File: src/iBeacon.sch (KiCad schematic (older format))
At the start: 7 parts, among them IC1 AE-TYBLE16, P1 CONN_01X02, P2 CONN_01X02, P3 CONN_01X02

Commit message: 2nd Version
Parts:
- added IC2: ATTINY10-TSHR, ATTINY10-TSHR:SOT95P280X145-6N, symbol ATTINY10-TSHR
- added JP1: JUMPER, solderjumper:SolderJumper-2_P1.3mm_Open_Pad1.0x1.5mm, symbol JUMPER
- added P4: CONN_01X03, Pin_Headers:Pin_Header_Angled_1x03_Pitch2.54mm, symbol CONN_01X03
- D1: footprint LEDs:LED_1206_HandSoldering -> LEDs:LED_0603_HandSoldering
- R1: footprint Resistors_SMD:R_1206_HandSoldering -> Resistors_SMD:R_0603_HandSoldering
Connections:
- net at Battery1.1 (P1), IC1.11 (+V), P1.1 (P1): now also IC2.5 (VCC)
- net at Battery1.2 (P2), D1.1 (K), IC1.12 (GND)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: now also IC2.2 (GND)
- net at IC1.2 (SWDI), P2.1 (P1): now also JP1.2
- new net: IC2.4 (PB2_(T0/CLKO/PCINT2/INT0/ADC2)), JP1.1
- new net: IC2.1 ((PCINT0/TPIDATA/OC0A/ADC0/AIN0)_PB0), P4.2 (P2)
- new net: IC2.3 ((PCINT1/TPICLK/CLKI/ICP0/OC0B/ADC1/AIN1)_PB1), P4.1 (P1)
- new net: IC2.6 (PB3_(~RESET~/PCINT3/ADC3)), P4.3 (P3)
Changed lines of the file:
@@
 LIBS:valves
 LIBS:ae-tyble16
+LIBS:ATTINY10-TSHR
 LIBS:iBeacon-cache
 EELAYER 25 0
@@
 NoConn ~ 5150 3300
 NoConn ~ 5150 3500
-Wire Wire Line
-	4250 3400 4150 3400
-Wire Wire Line
-	4150 3400 4150 3500
-Wire Wire Line
-	4150 3500 4250 3500
 $Comp
 L CONN_01X02 Battery1
@@
 	1    0    0    -1
 $EndComp
-Wire Wire Line
-	4250 3000 4100 3000
-Wire Wire Line
-	4100 3000 4100 3100
-Wire Wire Line
-	4100 3100 3950 3100
-Wire Wire Line
-	3950 3200 4250 3200
-Wire Wire Line
-	4250 3300 3950 3300
-Wire Wire Line
-	4000 2900 4250 2900
-Wire Wire Line
-	5150 3000 5650 3000
-Wire Wire Line
-	5150 3100 5650 3100
-Wire Wire Line
-	5300 2400 5250 2400
-Wire Wire Line
-	5250 2400 5250 3000
-Connection ~ 5250 3000
-Wire Wire Line
-	5300 2500 5200 2500
-Wire Wire Line
-	5200 2500 5200 3100
-Connection ~ 5200 3100
 $Comp
 L AE-TYBLE16 IC1
@@
 F 0 "R1" V 5430 3400 50  0000 C CNN
 F 1 "R" V 5350 3400 50  0000 C CNN
-F 2 "Resistors_SMD:R_1206_HandSoldering" V 5280 3400 50  0000 C CNN
+F 2 "Resistors_SMD:R_0603_HandSoldering" V 5280 3400 50  0000 C CNN
 F 3 "" H 5350 3400 50  0000 C CNN
 	1    5350 3400
@@
 F 0 "D1" H 5750 3500 50  0000 C CNN
 F 1 "LED" H 5750 3300 50  0000 C CNN
-F 2 "LEDs:LED_1206_HandSoldering" H 5800 3250 50  0000 C CNN
+F 2 "LEDs:LED_0603_HandSoldering" H 5800 3250 50  0000 C CNN
 F 3 "" H 5750 3400 50  0000 C CNN
 	1    5750 3400
 	-1   0    0    -1
 $EndComp
-Wire Wire Line
-	5150 3400 5200 3400
-Wire Wire Line
-	5500 3400 5550 3400
-Wire Wire Line
-	5950 3200 5950 3400
-Wire Wire Line
-	5500 3200 5950 3200
-Wire Wire Line
-	5500 3100 5500 3200
-Connection ~ 5500 3100
 $Comp
 L CONN_01X02 P3
@@
 	1    0    0    -1
 $EndComp
+$Comp
+L JUMPER JP1
+U 1 1 5CA0BF62
+P 3800 2400
+F 0 "JP1" H 3800 2550 50  0000 C CNN
+F 1 "JUMPER" H 3800 2320 50  0000 C CNN
+F 2 "solderjumper:SolderJumper-2_P1.3mm_Open_Pad1.0x1.5mm" H 3800 2400 50  0000 C CNN
+F 3 "" H 3800 2400 50  0000 C CNN
+	1    3800 2400
+	1    0    0    -1
+$EndComp
+$Comp
+L ATTINY10-TSHR IC2
+U 1 1 5CA0BFA7
+P 1800 1350
+F 0 "IC2" H 6050 1650 50  0000 L CNN
+F 1 "ATTINY10-TSHR" H 6050 1550 50  0000 L CNN
+F 2 "ATTINY10-TSHR:SOT95P280X145-6N" H 6050 1450 50  0001 L CNN
+F 3 "http://www.atmel.com/images/atmel-8127-avr-8-bit-microcontroller-attiny4-attiny5-attiny9-attiny10_datasheet.pdf" H 6050 1350 50  0001 L CNN
+F 4 "ATTINY10-TSHR, 8 bit AVR Microcontroller 12MHz 1024 B Flash, 32 B RAM, 6-Pin SOT-23" H 6050 1250 50  0001 L CNN "Description"
+F 5 "1.45" H 6050 1150 50  0001 L CNN "Height"
+F 6 "Microchip" H 6050 1050 50  0001 L CNN "Manufacturer_Name"
+F 7 "ATTINY10-TSHR" H 6050 950 50  0001 L CNN "Manufacturer_Part_Number"
+F 8 "556-ATTINY10-TSHR" H 6050 850 50  0001 L CNN "Mouser Part Number"
+F 9 "https://www.mouser.com/Search/Refine.aspx?Keyword=556-ATTINY10-TSHR" H 6050 750 50  0001 L CNN "Mouser Price/Stock"
+F 10 "1330946P" H 6050 650 50  0001 L CNN "RS Part Number"
+F 11 "http://uk.rs-online.com/web/p/products/1330946P" H 6050 550 50  0001 L CNN "RS Price/Stock"
+	1    1800 1350
+	1    0    0    -1
+$EndComp
+Wire Wire Line
+	4250 3400 4150 3400
+Wire Wire Line
+	4150 3400 4150 3500
+Wire Wire Line
+	4150 3500 4250 3500
+Wire Wire Line
+	4250 3000 4100 3000
+Wire Wire Line
+	4100 3000 4100 3100
+Wire Wire Line
+	4100 3100 3950 3100
+Wire Wire Line
+	3950 3200 4250 3200
+Wire Wire Line
+	4250 3300 3950 3300
+Wire Wire Line
+	4000 2900 4250 2900
+Wire Wire Line
+	5150 3000 5650 3000
+Wire Wire Line
+	5150 3100 5650 3100
+Wire Wire Line
+	5300 2400 5250 2400
+Wire Wire Line
+	5250 2400 5250 3000
+Connection ~ 5250 3000
+Wire Wire Line
+	5300 2500 5200 2500
+Wire Wire Line
+	5200 2500 5200 3100
+Connection ~ 5200 3100
+Wire Wire Line
+	5150 3400 5200 3400
+Wire Wire Line
+	5500 3400 5550 3400
+Wire Wire Line
+	5950 3200 5950 3400
+Wire Wire Line
+	5500 3200 6700 3200
+Wire Wire Line
+	5500 3100 5500 3200
+Connection ~ 5500 3100
 Wire Wire Line
 	4000 2900 4000 3000
 Wire Wire Line
 	4000 3000 3950 3000
+Wire Wire Line
+	4100 2400 4100 2900
+Connection ~ 4100 2900
+Wire Wire Line
+	3500 2400 3500 1800
+Wire Wire Line
+	3500 1800 6200 1800
+Wire Wire Line
+	6200 1800 6200 1550
+Wire Wire Line
+	6200 1450 6350 1450
+Wire Wire Line
+	6350 1450 6350 2200
+Wire Wire Line
+	6350 2200 5600 2200
+Wire Wire Line
+	5600 2200 5600 2900
+Wire Wire Line
+	5600 2900 5500 2900
+Wire Wire Line
+	5500 2900 5500 3000
+Connection ~ 5500 3000
+Wire Wire Line
+	6700 3200 6700 950
+Wire Wire Line
+	6700 950  1550 950
+Wire Wire Line
+	1550 950  1550 1450
+Wire Wire Line
+	1550 1450 1800 1450
+Connection ~ 5950 3200
+$Comp
+L CONN_01X03 P4
+U 1 1 5CA0C661
+P 1400 2150
+F 0 "P4" H 1400 2350 50  0000 C CNN
+F 1 "CONN_01X03" V 1500 2150 50  0000 C CNN
+F 2 "Pin_Headers:Pin_Header_Angled_1x03_Pitch2.54mm" H 1400 2150 50  0000 C CNN
+F 3 "" H 1400 2150 50  0000 C CNN
+	1    1400 2150
+	0    1    1    0
+$EndComp
+Wire Wire Line
+	1800 1350 1400 1350
+Wire Wire Line
+	1400 1350 1400 1950
+Wire Wire Line
+	1800 1550 1500 1550
+Wire Wire Line
+	1500 1550 1500 1950
+Wire Wire Line
+	6200 1350 6200 800
+Wire Wire Line
+	6200 800  1300 800
+Wire Wire Line
+	1300 800  1300 1950
 $EndSCHEMATC

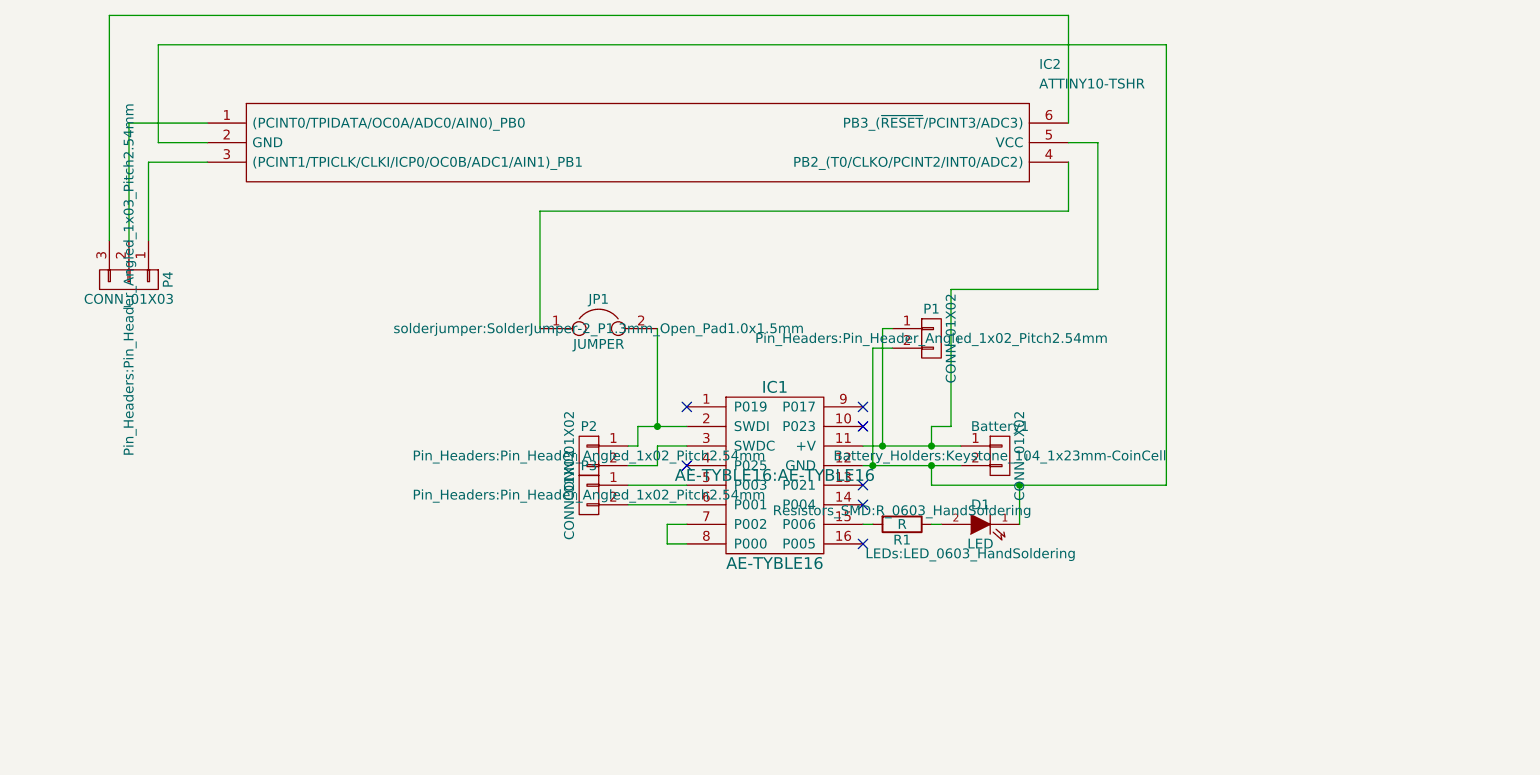
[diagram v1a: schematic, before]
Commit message: Redesigning board
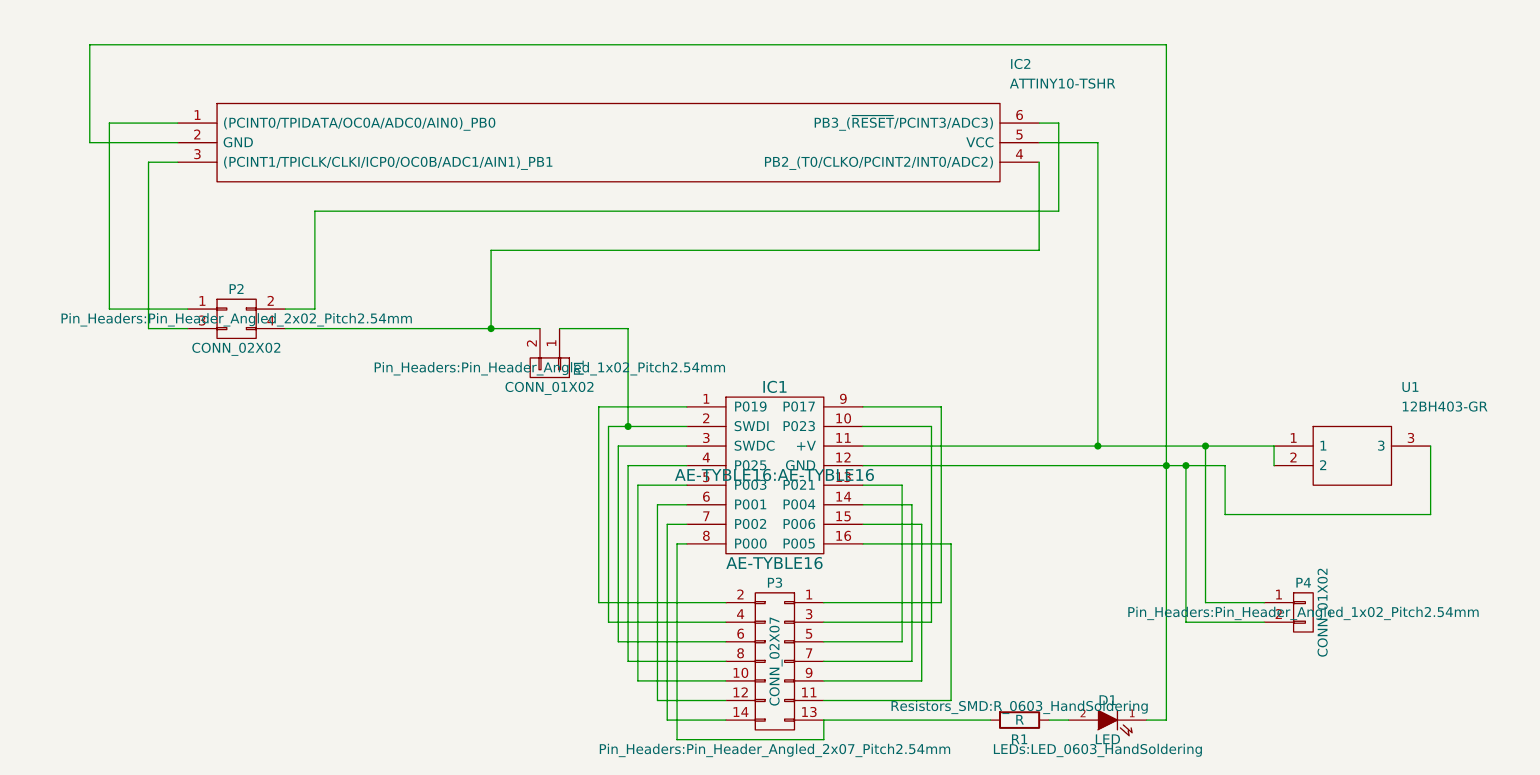
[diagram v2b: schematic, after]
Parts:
- removed Battery1: CONN_01X02, Battery_Holders:Keystone_104_1x23mm-CoinCell, symbol CONN_01X02
- removed JP1: JUMPER, solderjumper:SolderJumper-2_P1.3mm_Open_Pad1.0x1.5mm, symbol JUMPER
- removed P2, P3: CONN_01X02, Pin_Headers:Pin_Header_Angled_1x02_Pitch2.54mm, symbol CONN_01X02
- removed P4: CONN_01X03, Pin_Headers:Pin_Header_Angled_1x03_Pitch2.54mm, symbol CONN_01X03
- added P2: CONN_02X02, Pin_Headers:Pin_Header_Angled_2x02_Pitch2.54mm, symbol CONN_02X02
- added P3: CONN_02X07, Pin_Headers:Pin_Header_Angled_2x07_Pitch2.54mm, symbol CONN_02X07
- added P4: CONN_01X02, Pin_Headers:Pin_Header_Angled_1x02_Pitch2.54mm, symbol CONN_01X02
- added U1: 12BH403-GR, 12BH403GR, symbol 12BH403-GR
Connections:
- net at IC1.1 (P019): now also P3.2 (P2)
- net at IC1.10 (P023): now also P3.3 (P3)
- net at IC1.11 (+V), IC2.5 (VCC): now also P4.1 (P1), U1.1, U1.2; no longer P1.1 (P1)
- net at D1.1 (K), IC1.12 (GND), IC2.2 (GND): now also P4.2 (P2), U1.3; no longer P1.2 (P2)
- net at IC1.13 (P021): now also P3.5 (P5)
- net at IC1.14 (P004): now also P3.7 (P7)
- net at IC1.15 (P006): now also P3.9 (P9); no longer R1.2
- net at IC1.16 (P005): now also P3.11 (P11)
- net at IC1.2 (SWDI): now also P1.1 (P1), P3.4 (P4)
- net at IC1.3 (SWDC): now also P3.6 (P6)
- net at IC1.4 (P025): now also P3.8 (P8)
- net at IC1.5 (P003): now also P3.10 (P10)
- net at IC1.6 (P001): now also P3.12 (P12)
- net at IC1.7 (P002): now also P3.14 (P14); no longer IC1.8 (P000)
- net at IC1.9 (P017): now also P3.1 (P1)
- net at IC2.4 (PB2_(T0/CLKO/PCINT2/INT0/ADC2)): now also P1.2 (P2), P2.4 (P4)
- net at IC2.1 ((PCINT0/TPIDATA/OC0A/ADC0/AIN0)_PB0): now also P2.1 (P1)
- net at IC2.3 ((PCINT1/TPICLK/CLKI/ICP0/OC0B/ADC1/AIN1)_PB1): now also P2.3 (P3)
- net at IC2.6 (PB3_(~RESET~/PCINT3/ADC3)): now also P2.2 (P2)
- new net: IC1.8 (P000), P3.13 (P13), R1.2
- no-connect marks 7 -> 0
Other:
- moved on the sheet: D1, IC2, R1
